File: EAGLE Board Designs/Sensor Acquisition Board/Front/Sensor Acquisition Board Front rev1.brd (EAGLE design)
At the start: 92.7 x 50.8 mm, 38 parts, among them J1 CONNECTOR-SENSOR_NF_S_RA_BLACK, J10 JUMPER_0603_, J2 CONNECTOR-SENSOR_NF_S_RA_BLACK, J3 CONNECTOR-CAN_NF_S_RA_BLACK, J4 CONNECTOR-CAN_NF_S_RA_BLACK, J6 JUMPER_0603_, U1 VOLTAGE_REGULATOR_SOT-223_5V, U2 MCP2562FD, U3 MCP2562FD

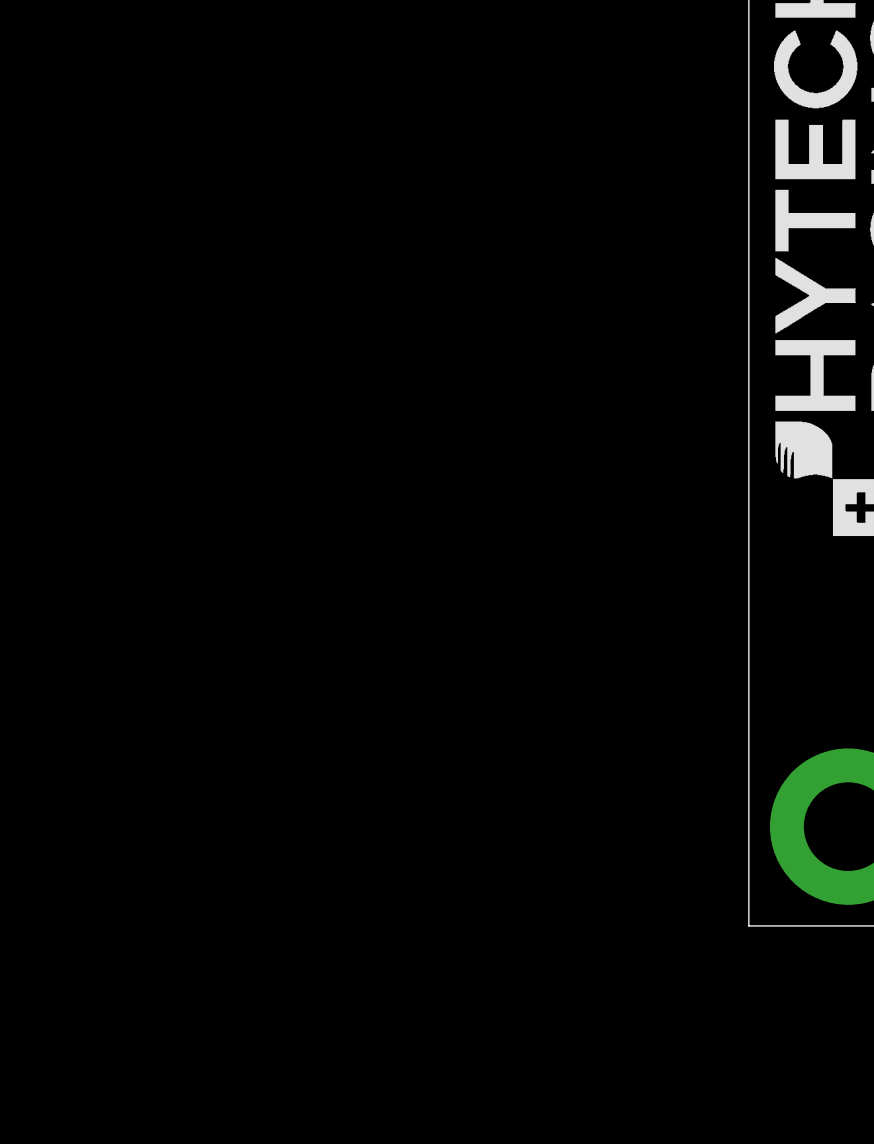
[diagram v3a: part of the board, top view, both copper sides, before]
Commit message: connect Ultimate GPS to SAB Front Teensy
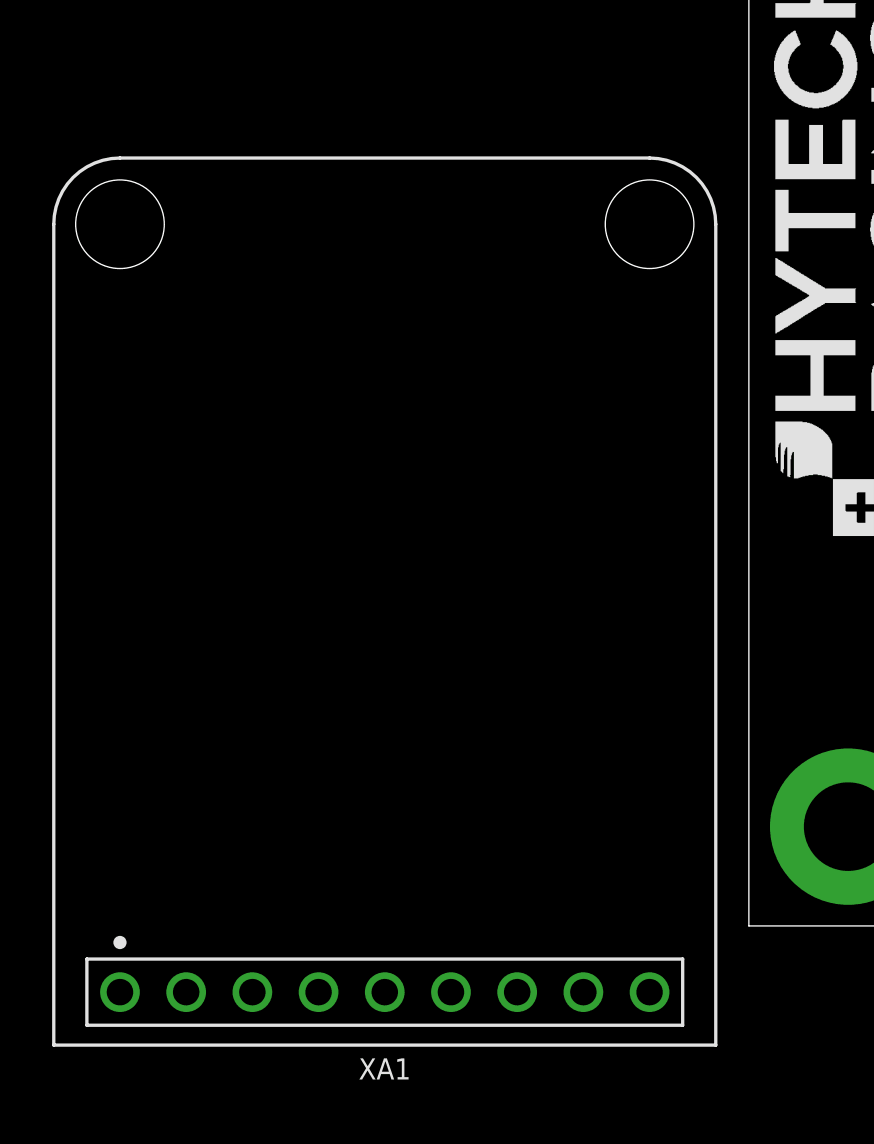
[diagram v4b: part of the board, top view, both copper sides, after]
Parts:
- added XA1: ULTIMATE_GPS, HyTechDevices:ULTIMATE_GPS
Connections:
- new net GPS_RX: A2.D7, XA1.RX
- new net GPS_TX: A2.D8, XA1.TX
- new net VBAT: XA1.VBAT
- new net VIN: XA1.VIN
- net GND: now also XA1.GND
- net TEENSY_3.3V: now also XA1.3.3V
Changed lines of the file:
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@@
 </element>
 <element name="U$7" library="HyTechManufacturing" package="LOGO_HYTECH_MEDIUM" value="" x="7.62" y="12.7" smashed="yes" rot="R90"/>
+<element name="XA1" library="HyTechDevices" package="ULTIMATE_GPS" value="ULTIMATE_GPS" x="-13.97" y="-2.54" smashed="yes">
+<attribute name="DKPN" value="DW-09-07-G-S-200-ND" x="-13.97" y="-2.54" size="1.778" layer="27" display="off"/>
+<attribute name="MANUFACTURER" value="Samtec Inc." x="-13.97" y="-2.54" size="1.778" layer="27" display="off"/>
+<attribute name="MOPN" value="200-DW0907GS200" x="-13.97" y="-2.54" size="1.778" layer="27" display="off"/>
+<attribute name="MPN" value="DW-09-07-G-S-200" x="-13.97" y="-2.54" size="1.778" layer="27" display="off"/>
+<attribute name="NAME" x="-13.97" y="-5.08" size="0.8128" layer="25" font="vector" rot="R180" align="bottom-center"/>
+</element>
 </elements>
 <signals>
@@
 <wire x1="66.04" y1="19.05" x2="72.79" y2="19.05" width="0.254" layer="1"/>
 <wire x1="72.79" y1="19.05" x2="74.95" y2="16.89" width="0.254" layer="1"/>
+<contactref element="XA1" pad="GND"/>
+<wire x1="-8.89" y1="-2.54" x2="15.26" y2="16.89" width="0" layer="19" extent="1-1"/>
 </signal>
 <signal name="+5V">
@@
 <wire x1="70.1121" y1="30.7894" x2="64.961425" y2="30.7894" width="0.254" layer="1"/>
 <wire x1="58.42" y1="29.21" x2="55.88" y2="26.67" width="0.254" layer="16"/>
+<contactref element="XA1" pad="3.3V"/>
+<wire x1="-24.13" y1="-2.54" x2="21.59" y2="45.72" width="0" layer="19" extent="1-1"/>
 </signal>
 <signal name="SENSOR_1">
@@
 <wire x1="78.105" y1="27.305" x2="79.16" y2="28.36" width="0.254" layer="1"/>
 </signal>
+<signal name="VIN">
+<contactref element="XA1" pad="VIN"/>
+</signal>
+<signal name="VBAT">
+<contactref element="XA1" pad="VBAT"/>
+</signal>
+<signal name="GPS_RX">
+<contactref element="XA1" pad="RX"/>
+<contactref element="A2" pad="D7"/>
+<wire x1="-11.43" y1="-2.54" x2="36.83" y2="30.48" width="0" layer="19" extent="1-1"/>
+</signal>
+<signal name="GPS_TX">
+<contactref element="XA1" pad="TX"/>
+<contactref element="A2" pad="D8"/>
+<wire x1="-13.97" y1="-2.54" x2="39.37" y2="30.48" width="0" layer="19" extent="1-1"/>
+</signal>
 </signals>

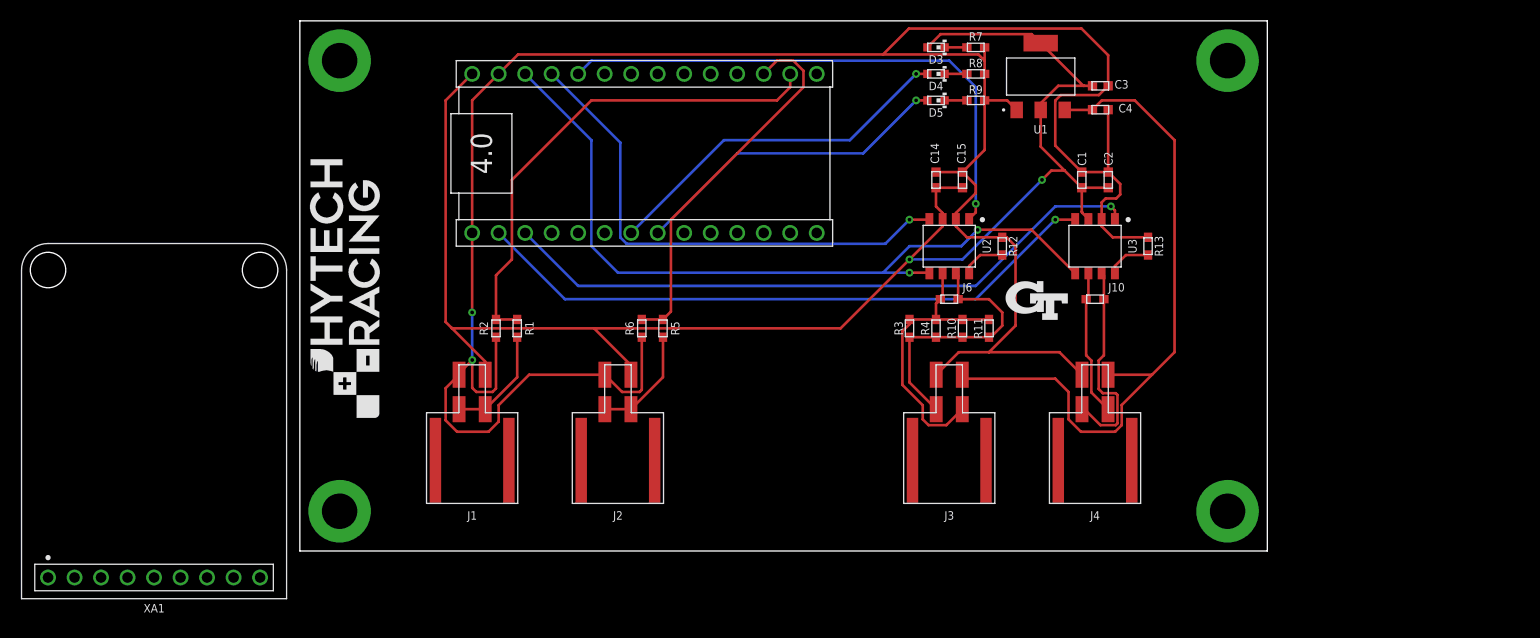
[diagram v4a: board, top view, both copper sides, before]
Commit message: Created GPS LED and added GPS to Board
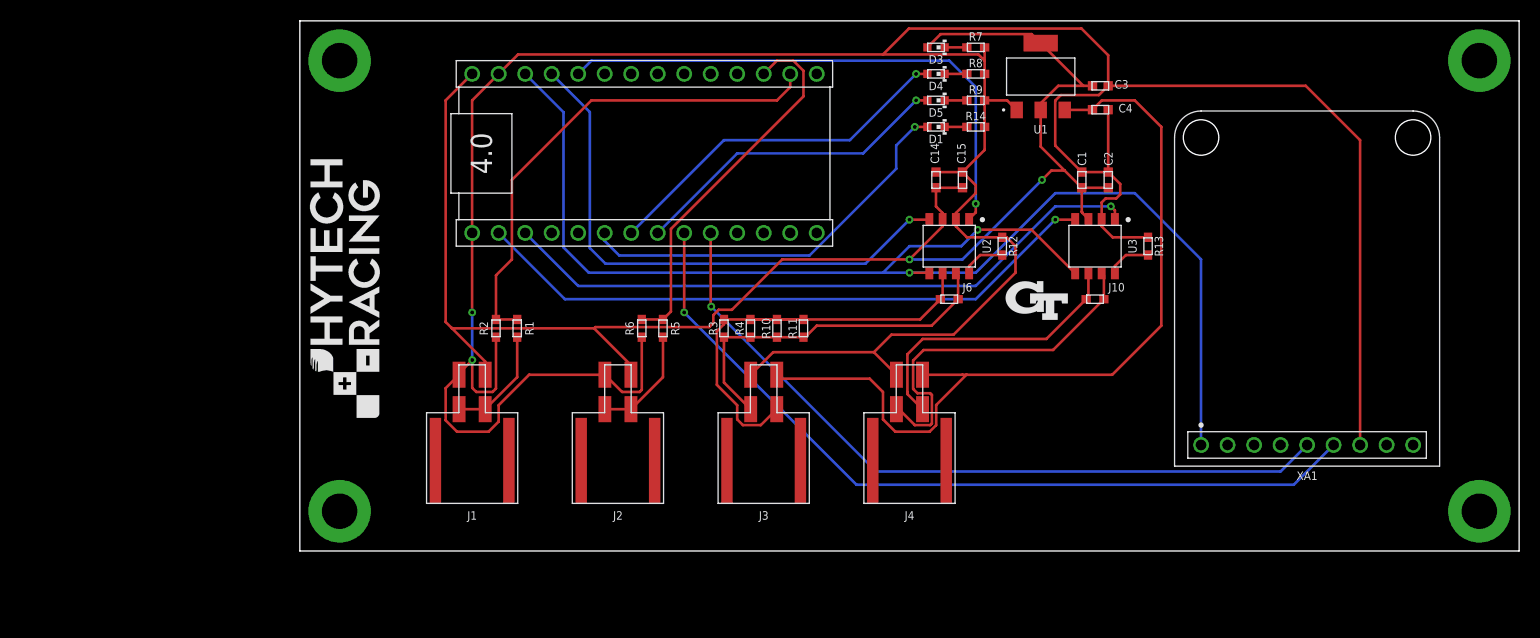
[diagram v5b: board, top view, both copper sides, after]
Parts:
- added D1: LED_0603_RED, HyTechDevices:0603-LED
- added R14: RESISTOR_0603_470, HyTechDevices:0603-RES
- moved XA1 111.2 mm to (96.5, 10.2)
- moved U$1 24.1 mm to (113.0, 3.81)
- moved U$4 24.1 mm to (113.0, 47.0)
- moved R11 17.8 mm to (48.3, 21.3)
- moved J4 17.8 mm to (58.4, 15.2)
- moved R10 17.8 mm to (45.7, 21.3)
- moved R3 17.8 mm to (40.6, 21.3)
- moved R4 17.8 mm to (43.2, 21.3)
- moved J3 17.8 mm to (44.5, 15.2)
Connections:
- new net GPS_LED: A2.D4, D1.2
- new net N$4: D1.1, R14.1
- net GND: now also R14.2
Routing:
- net GPS_RX: track 0.00 -> 78.3 mm, vias 0 -> 1
- net GPS_TX: track 0.00 -> 71.8 mm, vias 0 -> 1
- net GND: track 240.7 -> 304.2 mm
- net TEENSY_3.3V: track 74.5 -> 127.6 mm
- net GPS_LED: track 0.00 -> 38.7 mm, vias 0 -> 1
- net CANL1: track 27.6 -> 44.5 mm
- net CANH: track 20.2 -> 34.9 mm
- net +12V: track 65.4 -> 79.9 mm
- net CANL: track 14.0 -> 27.7 mm
- net CANH1: track 25.9 -> 34.5 mm
- net CANRX1: track 49.2 -> 53.1 mm
- net N$4: track 0.00 -> 2.14 mm
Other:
- board size 92.7 x 50.8 mm -> 116.8 x 50.8 mm

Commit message: Fixed front
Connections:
- net GPS_LED: now also XA1.FIX; no longer A2.D4
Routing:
- net GPS_LED: track 38.7 -> 54.7 mm
- net GND: track 304.2 -> 306.3 mm
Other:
- board text added: "GPS"
- board text added: "HyTech Racing 2022 Sensor Acquisition Board Front rev1 Designed by Bo Han Zhu"
- board text removed: "HyTech Racing 2022 Sensor Acquisition Board rev4 Designed by Bo Han Zhu"
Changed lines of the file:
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@@
 <wire x1="0" y1="50.8" x2="0" y2="0" width="0" layer="20"/>
 <text x="114.554" y="12.573" size="1.016" layer="51" font="vector" rot="R90">HyTech Racing 2022
-Sensor Acquisition Board rev4
+Sensor Acquisition Board Front rev1
 Designed by Bo Han Zhu</text>
 <text x="52.578" y="3.175" size="0.8128" layer="51" rot="R90">Vehicle CAN-Bus</text>
@@
 <text x="38.608" y="3.175" size="0.8128" layer="51" rot="R90">IMU CAN-Bus</text>
 <text x="58.42" y="43.18" size="0.8128" layer="51" rot="R180">Vehicle CAN</text>
+<text x="58.42" y="40.64" size="0.8128" layer="51" rot="R180">GPS</text>
 </plain>
 <attributes>
@@
 <wire x1="65.62" y1="43.18" x2="67.779" y2="43.18" width="0.254" layer="1"/>
 <wire x1="67.779" y1="43.18" x2="68.693" y2="42.266" width="0.254" layer="1"/>
-<wire x1="63.5" y1="36.31" x2="65.62" y2="38.43" width="0.254" layer="1"/>
+<wire x1="63.5" y1="36.31" x2="65.786" y2="36.31" width="0.254" layer="1"/>
+<wire x1="66.509" y1="37.033" x2="65.786" y2="36.31" width="0.254" layer="1"/>
 <wire x1="60.96" y1="36.31" x2="63.5" y2="36.31" width="0.254" layer="1"/>
 <wire x1="62.865" y1="31.8135" x2="62.865" y2="32.385" width="0.254" layer="1"/>
@@
 <contactref element="XA1" pad="GND"/>
 <contactref element="R14" pad="2"/>
-<wire x1="65.62" y1="38.43" x2="65.62" y2="40.64" width="0.254" layer="1"/>
+<wire x1="66.509" y1="39.751" x2="65.62" y2="40.64" width="0.254" layer="1"/>
+<wire x1="66.509" y1="39.751" x2="66.509" y2="37.033" width="0.254" layer="1"/>
 <wire x1="65.62" y1="43.18" x2="65.62" y2="40.64" width="0.254" layer="1"/>
 <wire x1="55.01" y1="19.05" x2="56.6864" y2="20.7264" width="0.254" layer="1"/>
@@
 <wire x1="93.98" y1="7.62" x2="96.52" y2="10.16" width="0.254" layer="16"/>
 </signal>
-<signal name="GPS_LED">
-<contactref element="A2" pad="D4"/>
-<contactref element="D1" pad="2"/>
-<wire x1="30.607" y1="28.321" x2="29.21" y2="29.718" width="0.254" layer="16"/>
-<wire x1="29.21" y1="30.48" x2="29.21" y2="29.718" width="0.254" layer="16"/>
-<wire x1="48.8437625" y1="28.321" x2="57.15" y2="36.6272375" width="0.254" layer="16"/>
-<wire x1="57.15" y1="38.862" x2="58.928" y2="40.64" width="0.254" layer="16"/>
-<via x="58.928" y="40.64" extent="1-16" drill="0.3556"/>
-<wire x1="58.928" y1="40.64" x2="60.135" y2="40.64" width="0.254" layer="1"/>
-<wire x1="30.607" y1="28.321" x2="48.8437625" y2="28.321" width="0.254" layer="16"/>
-<wire x1="57.15" y1="36.6272375" x2="57.15" y2="38.862" width="0.254" layer="16"/>
-</signal>
 <signal name="N$4">
 <contactref element="D1" pad="1"/>
@@
 <wire x1="61.785" y1="40.64" x2="63.92" y2="40.64" width="0.254" layer="1"/>
 </signal>
+<signal name="GPS_LED">
+<contactref element="D1" pad="2"/>
+<contactref element="XA1" pad="FIX"/>
+<wire x1="93.98" y1="10.16" x2="93.98" y2="24.13" width="0.1524" layer="16"/>
+<wire x1="93.98" y1="24.13" x2="78.74" y2="39.37" width="0.1524" layer="16"/>
+<via x="65.7978" y="39.37" extent="1-16" drill="0.3556"/>
+<wire x1="65.7978" y1="39.37" x2="61.405" y2="39.37" width="0.1524" layer="1"/>
+<wire x1="61.405" y1="39.37" x2="60.135" y2="40.64" width="0.1524" layer="1"/>
+<wire x1="78.74" y1="39.37" x2="65.7978" y2="39.37" width="0.1524" layer="16"/>
+</signal>
 </signals>
